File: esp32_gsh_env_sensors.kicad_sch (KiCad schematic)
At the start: 45 parts, among them J1 USB_C_Receptacle_USB2.0, Q1 SS8050, Q2 SS8050, SW1 EN, SW2 BOOT, U1 MP2359, U2 CH340G, U3 ESP32-WROOM-32E, U4 MH-Z19B, U5 BME280, Y1 12MHz

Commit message: Update schematics
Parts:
- added J3: Conn_01x05_Male, symbol Connector:Conn_01x05_Male
- added J5: Conn_01x04_Male, symbol Connector:Conn_01x04_Male
- J2: renamed from J?; value Conn_01x05_Female -> C50950
- J4: renamed from J?; value Conn_01x04_Female -> C2718488
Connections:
- net GND: now also C13.2, J4.3 (Pin_3); no longer C13.1, U4.7 (GND)
- net IO16/TXD: now also J2.3 (Pin_3); no longer U4.3 (TXD)
- net IO17/RXD: now also J2.2 (Pin_2); no longer U4.2 (RXD)
- net VBUS: now also C13.1, J4.4 (Pin_4); no longer C13.2, U4.6 (Vin)
- net MH-Z19B Vout: now reaches U4.1 (Vout)
- net MH-Z19B Vout: now also J3.1 (Pin_1)
- net MH-Z19B HD: now reaches U4.5 (HD)
- net MH-Z19B HD: now also J3.5 (Pin_5)
- net IO15/PWM: now reaches J4.1 (Pin_1)
- net IO15/PWM: now also U3.29 (GPIO5)
- net PWM renamed MH-Z19B PWM
- net MH-Z19B PWM: now also J5.1 (Pin_1); no longer U3.29 (GPIO5)
- new net MH-Z19B A0T: J5.2 (Pin_2)
- new net MH-Z19B GND: J5.3 (Pin_3), U4.7 (GND)
- new net MH-Z19B RXD: J3.2 (Pin_2), U4.2 (RXD)
- new net MH-Z19B SR: J3.4 (Pin_4)
- new net MH-Z19B TXD: J3.3 (Pin_3), U4.3 (TXD)
- new net MH-Z19B Vin: J5.4 (Pin_4), U4.6 (Vin)
- no-connect marks 30 -> 32
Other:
- moved on the sheet: C11, C12, C13, C14, C15, D3, J2, J4, R11, R12, U3, U4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

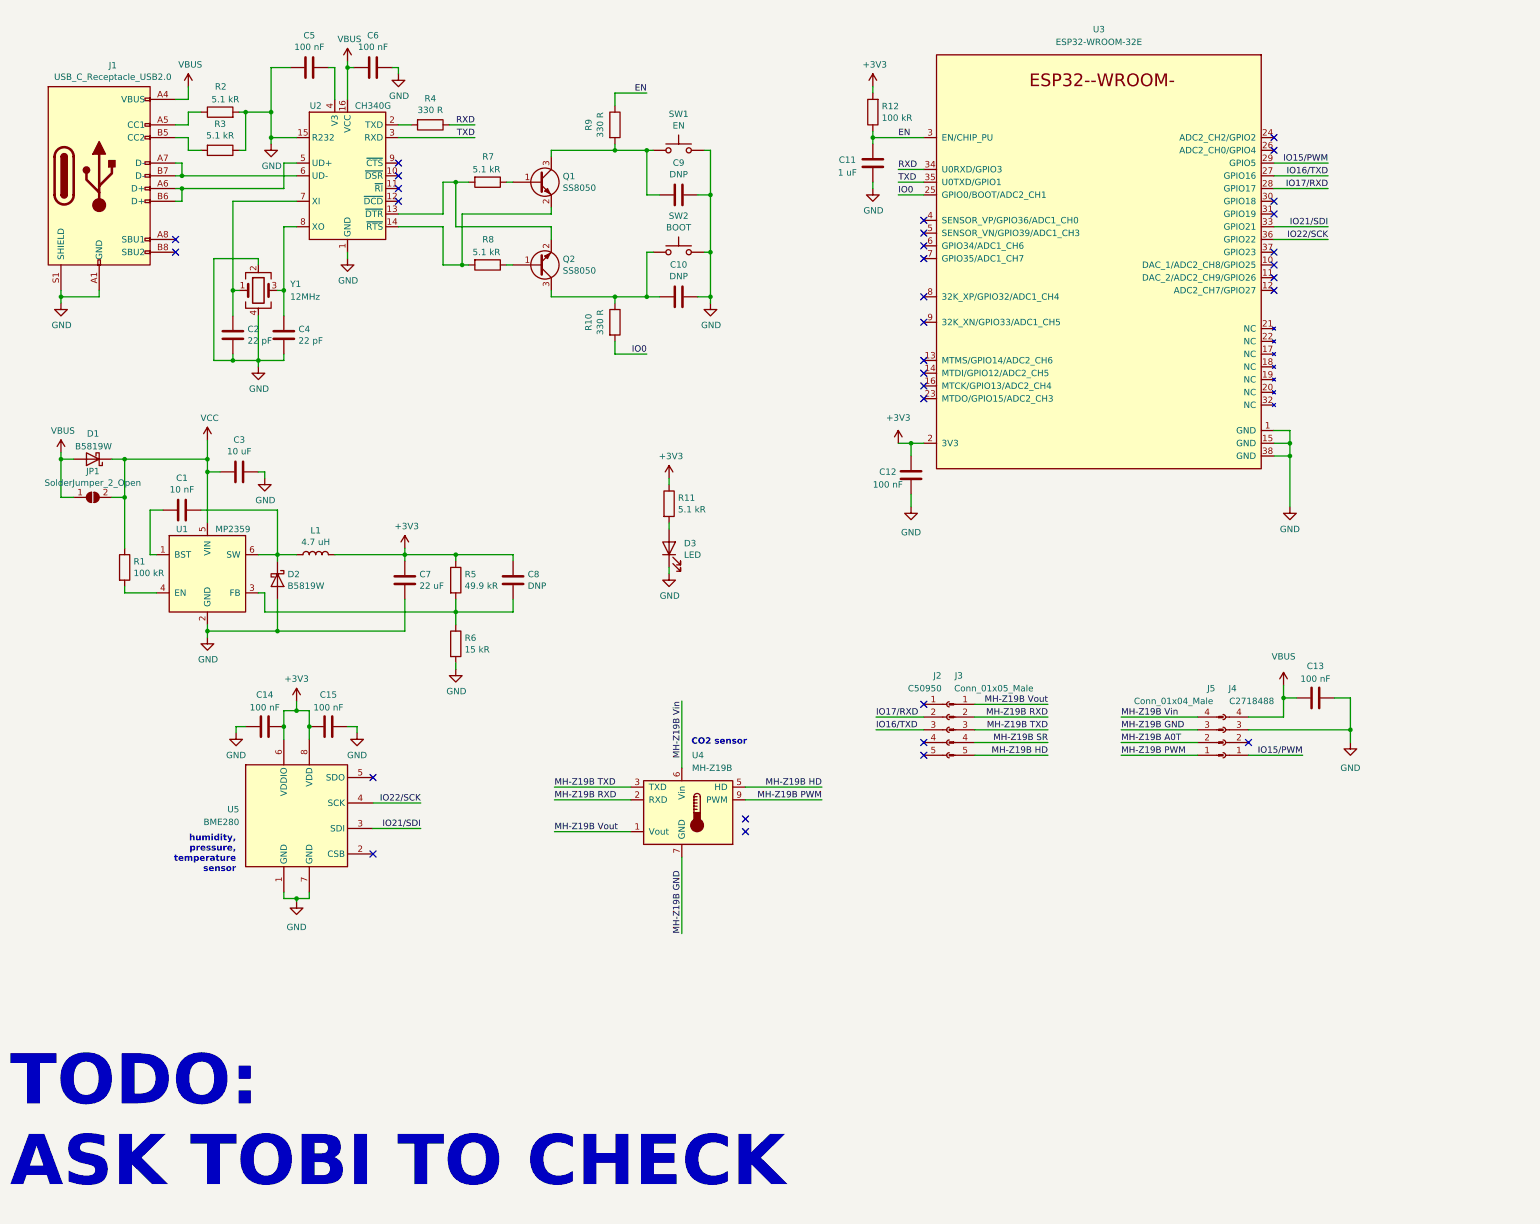
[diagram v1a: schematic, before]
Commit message: Multiple fixes, see below
- Change CH340G to 3.3V power source
- Fix floating pins (CSB, SDO) for BME280
- Add pull up resistors to BME280s SCK and SDI pins
- Fix naming of GPIO5 net (previously IO15/PWM, now IO5/PWM)
- Add switch to pull down MH-Z19Bs 'HD' pin for calibration
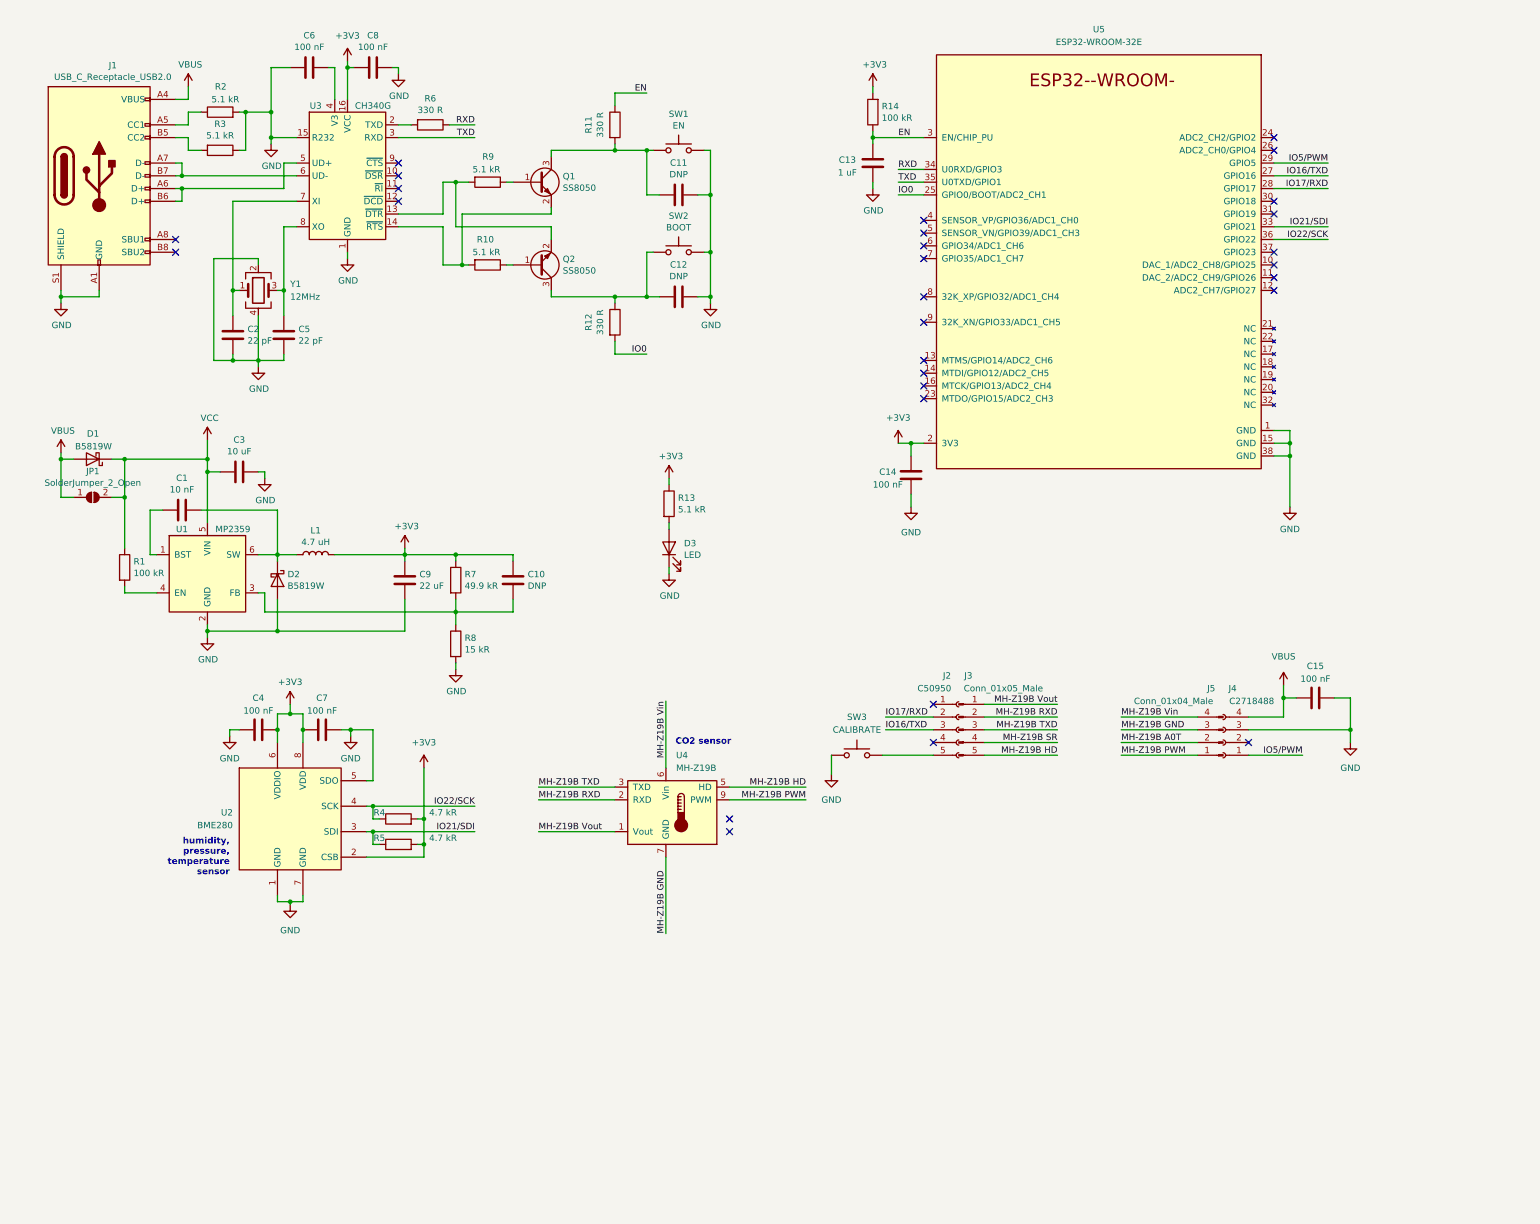
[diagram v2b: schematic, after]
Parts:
- added R4, R5: 4.7 kR, symbol Device:R
- added SW3: CALIBRATE, symbol Switch:SW_Push
- renumbered C8 to C10, C9 to C11, C10 to C12, C11 to C13, C12 to C14, C13 to C15, C14 to C4, C4 to C5, C5 to C6, C15 to C7, C6 to C8, C7 to C9, R8 to R10, R9 to R11, R10 to R12, R11 to R13, R12 to R14, R4 to R6, R5 to R7, R6 to R8, R7 to R9, U5 to U2, U2 to U3, U3 to U5
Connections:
- net +3V3: now also C8.2, U2.2 (CSB), U3.16 (VCC), R4.2, R5.2
- net GND: now also U2.5 (SDO), SW3.1
- net IO21/SDI: now also R5.1
- net IO22/SCK: now also R4.1
- net VBUS: no longer C8.2, U3.16 (VCC)
- net at J2.5 (Pin_5): now also SW3.2
- net IO15/PWM renamed IO5/PWM
- no-connect marks 32 -> 29
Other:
- note removed: "TODO: ASK TOBI TO CHECK"
- moved on the sheet: C4, C7, J2, J3, U2, U4

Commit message: Fix ch340 3.3V input; Add 5.1kR to protect ESP32; Add PWR_FLAG to schematics
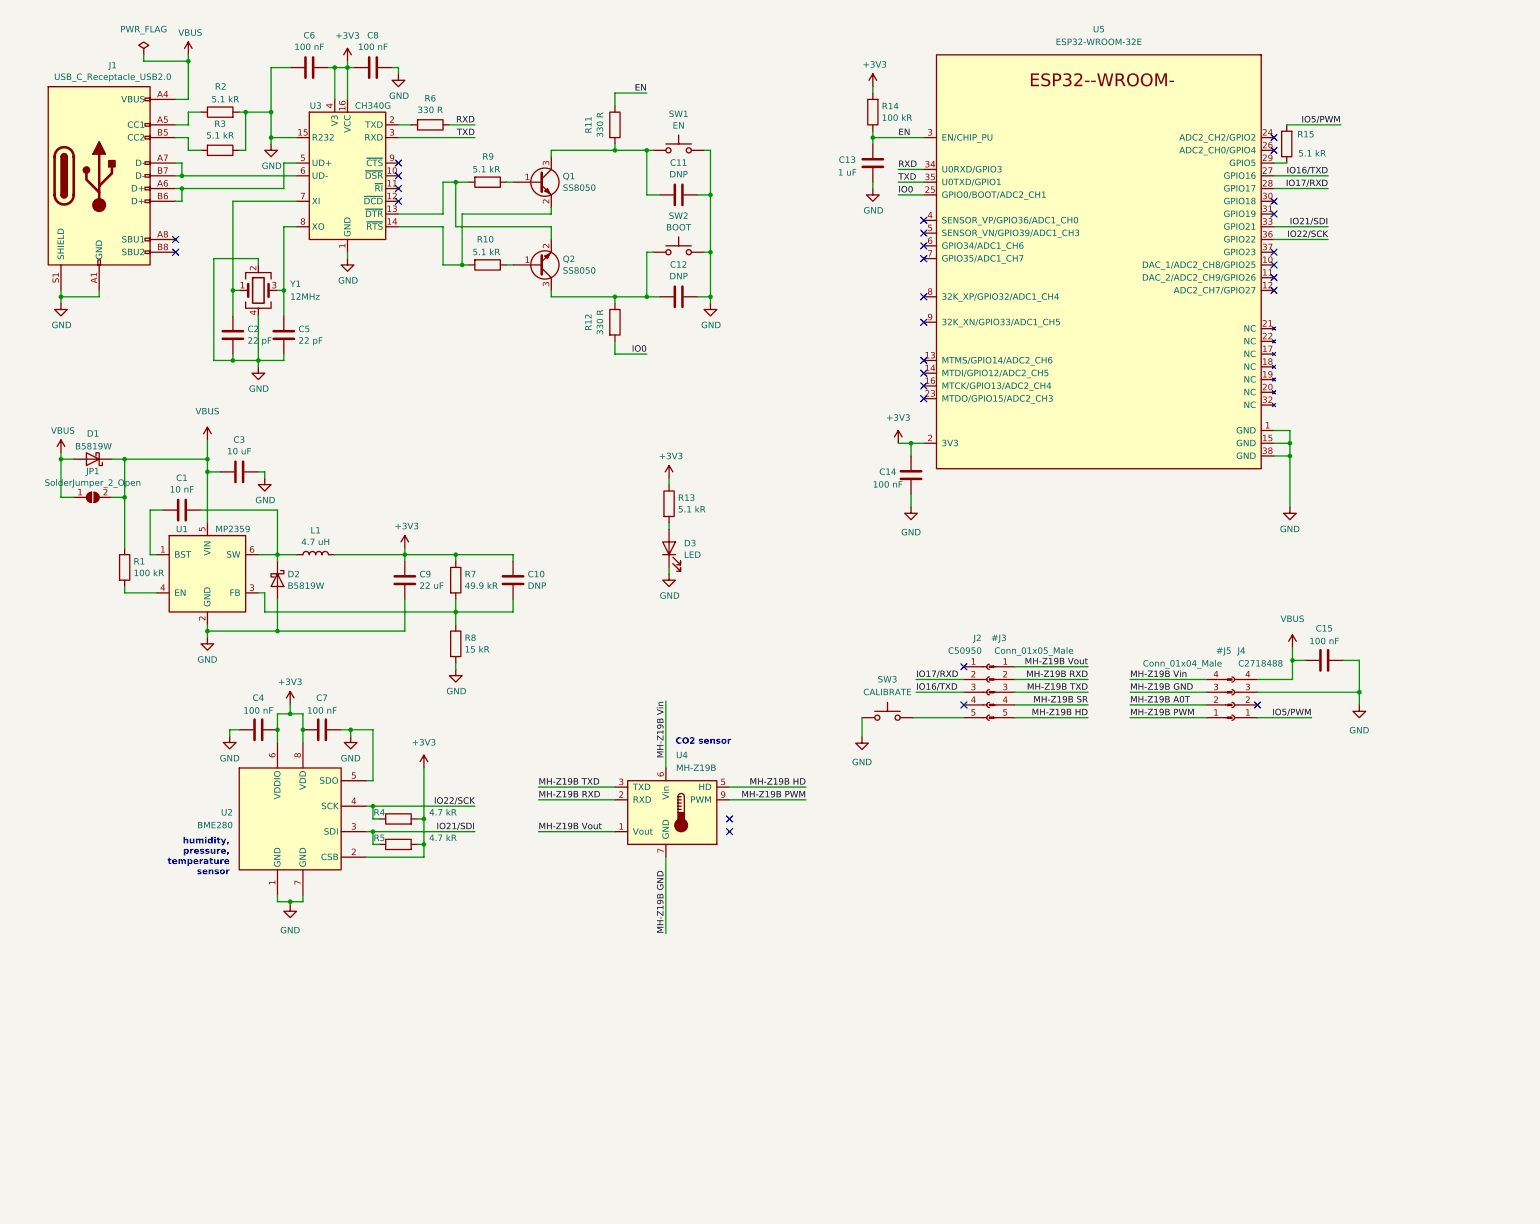
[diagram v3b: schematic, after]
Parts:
- added R15: 5.1 kR, symbol Device:R
- J2: LCSC (none) -> C50950
- J4: LCSC (none) -> C2718488
- renumbered J3 to #J3, J5 to #J5
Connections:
- net VCC is gone; now on net VBUS: C3.2, D1.1 (K), JP1.2 (B), R1.1, U1.5 (VIN)
- net +3V3: now also C6.1, U3.4 (V3)
- net IO5/PWM: now also R15.2; no longer U5.29 (GPIO5)
- new net: R15.1, U5.29 (GPIO5)
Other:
- moved on the sheet: C15, J2, J4, SW3

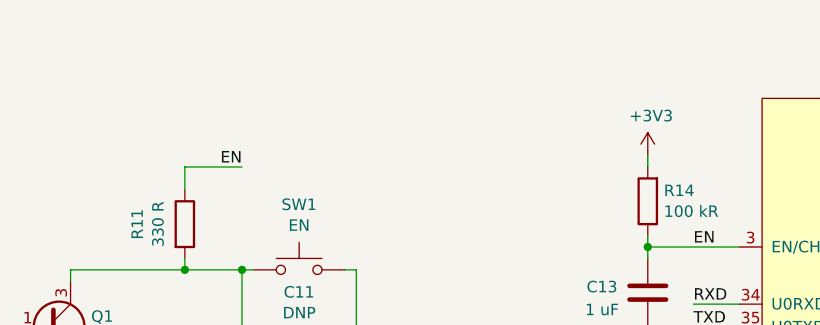
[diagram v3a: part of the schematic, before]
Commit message: Get schmeatics ready for layouting
- Add OSHW logo
- Add manufacturing mounting holes
- Assign footprints
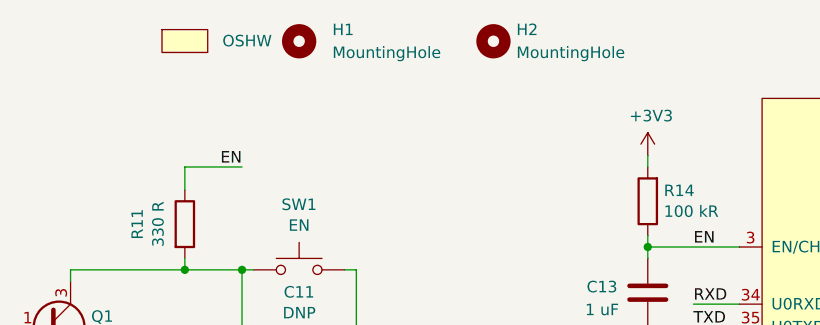
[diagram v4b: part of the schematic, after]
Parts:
- added H1, H2: MountingHole, ToolingHole:ToolingHole_JLCSMT, symbol Mechanical:MountingHole
- added I1: OSHW, Symbol:OSHW-Logo2_9.8x8mm_SilkScreen, symbol Icon:Icon
- C10, C11, C12: footprint Capacitor_SMD:C_0402_1005Metric -> Capacitor_SMD:C_0402_1005Metric_Pad0.74x0.62mm_HandSolder
- C14, C15, C4, C7: footprint (none) -> Capacitor_SMD:C_0402_1005Metric
- J2: footprint (none) -> Connector_PinSocket_2.54mm:PinSocket_1x05_P2.54mm_Vertical
- J4: footprint (none) -> Connector_PinSocket_2.54mm:PinSocket_1x04_P2.54mm_Vertical
- R15, R4, R5: footprint (none) -> Resistor_SMD:R_0402_1005Metric
- SW3: footprint (none) -> Button_Switch_SMD:SW_Push_SPST_NO_Alps_SKRK

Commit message: Add LSCS part numbers where available
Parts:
- C14, C15, C4, C7: LCSC (none) -> C1525
- R10, R13, R2, R3, R9: LCSC C25905 -> C25905
- R15: LCSC (none) -> C25905
- R4, R5: LCSC (none) -> C25900
- SW3: LCSC (none) -> C115357
- U2: LCSC (none) -> C92489
- U5: LCSC (none) -> C701343
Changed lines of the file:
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@@
+      (effects (font (size 1.27 1.27)) hide)
+    )
+    (property "LCSC" "C25900" (id 4) (at 86.36 179.07 0)
       (effects (font (size 1.27 1.27)) hide)
     )
@@
       (effects (font (size 1.27 1.27)) hide)
     )
+    (property "LCSC" "C25905" (id 4) (at 263.525 39.37 0)
+      (effects (font (size 1.27 1.27)) hide)
+    )
     (pin "1")
     (pin "2")
@@
       (effects (font (size 1.27 1.27)) hide)
     )
+    (property "LCSC" "C115357" (id 4) (at 183.896 153.797 0)
+      (effects (font (size 1.27 1.27)) hide)
+    )
     (pin "1")
     (pin "2")
@@
     )
     (property "Datasheet" "https://www.espressif.com/sites/default/files/documentation/esp32-wroom-32e_esp32-wroom-32ue_datasheet_en.pdf" (id 3) (at 235.585 63.5 0)
+      (effects (font (size 1.27 1.27)) hide)
+    )
+    (property "LCSC" "C701343" (id 4) (at 225.425 63.5 0)
       (effects (font (size 1.27 1.27)) hide)
     )
@@
       (effects (font (size 1.27 1.27)) hide)
     )
+    (property "LCSC" "C25900" (id 4) (at 86.36 173.99 0)
+      (effects (font (size 1.27 1.27)) hide)
+    )
     (pin "1")
     (pin "2")
@@
       (effects (font (size 1.27 1.27)) hide)
     )
-    (property "LCSC" " C25905" (id 4) (at 50.8 40.64 0)
+    (property "LCSC" "C25905" (id 4) (at 50.8 40.64 0)
       (effects (font (size 1.27 1.27)) hide)
     )
@@
       (effects (font (size 1.27 1.27)) hide)
     )
-    (property "LCSC" " C25905" (id 4) (at 50.8 33.02 0)
+    (property "LCSC" "C25905" (id 4) (at 50.8 33.02 0)
       (effects (font (size 1.27 1.27)) hide)
     )
@@
       (effects (font (size 1.27 1.27)) hide)
     )
+    (property "LCSC" "C1525" (id 4) (at 71.12 156.21 0)
+      (effects (font (size 1.27 1.27)) hide)
+    )
     (pin "1")
     (pin "2")
@@
       (effects (font (size 1.27 1.27)) hide)
     )
+    (property "LCSC" "C1525" (id 4) (at 188.595 105.41 0)
+      (effects (font (size 1.27 1.27)) hide)
+    )
     (pin "1")
     (pin "2")
@@
       (effects (font (size 1.27 1.27)) hide)
     )
-    (property "LCSC" " C25905" (id 4) (at 104.14 63.5 0)
+    (property "LCSC" "C25905" (id 4) (at 104.14 63.5 0)
       (effects (font (size 1.27 1.27)) hide)
     )
@@
       (effects (font (size 1.27 1.27)) hide)
     )
-    (property "LCSC" " C25905" (id 4) (at 140.335 111.125 0)
+    (property "LCSC" "C25905" (id 4) (at 140.335 111.125 0)
       (effects (font (size 1.27 1.27)) hide)
     )
@@
       (effects (font (size 1.27 1.27)) hide)
     )
-    (property "LCSC" " C25905" (id 4) (at 104.14 46.99 0)
+    (property "LCSC" "C25905" (id 4) (at 104.14 46.99 0)
       (effects (font (size 1.27 1.27)) hide)
     )
@@
     )
     (property "Datasheet" "~" (id 3) (at 58.42 156.21 0)
+      (effects (font (size 1.27 1.27)) hide)
+    )
+    (property "LCSC" "C1525" (id 4) (at 58.42 156.21 0)
       (effects (font (size 1.27 1.27)) hide)
     )
@@
       (effects (font (size 1.27 1.27)) hide)
     )
+    (property "LCSC" "C1525" (id 4) (at 271.018 142.367 0)
+      (effects (font (size 1.27 1.27)) hide)
+    )
     (pin "1")
     (pin "2")
@@
       (effects (font (size 1.27 1.27)) hide)
     )
-    (property "Datasheet" "" (id 3) (at 109.22 126.365 0)
+    (property "Datasheet" "~" (id 3) (at 109.22 126.365 0)
       (effects (font (size 1.27 1.27)) hide)
     )
@@
       (effects (font (size 1.27 1.27)) hide)
     )
+    (property "LCSC" "C92489" (id 4) (at 64.77 173.99 0)
+      (effects (font (size 1.27 1.27)) hide)
+    )

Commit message: Fix title
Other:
- title: GSH ESP32 environment sensor -> GSH ESP32 environment sensors
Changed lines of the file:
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@@
   (paper "A4")
   (title_block
-    (title "GSH ESP32 environment sensor")
+    (title "GSH ESP32 environment sensors")
     (date "2022-02-24")
     (rev "A")

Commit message: Fix LED and MH-Z19B footprints
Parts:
- D3: footprint LED_SMD:LED_0603_1608Metric_Castellated -> LED_SMD:LED_0603_1608Metric
- U4: footprint sensor_Carbon_dioxide:mh-z19b -> mh-z19b:Winsen_MH-Z19B
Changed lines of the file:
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@@
       (effects (font (size 1.27 1.27)) (justify left))
     )
-    (property "Footprint" "sensor_Carbon_dioxide:mh-z19b" (id 2) (at 139.7 189.23 0)
+    (property "Footprint" "mh-z19b:Winsen_MH-Z19B" (id 2) (at 139.7 189.23 0)
       (effects (font (size 1.27 1.27)) hide)
     )
@@
       (effects (font (size 1.27 1.27)) (justify right))
     )
-    (property "Footprint" "LED_SMD:LED_0603_1608Metric_Castellated" (id 2) (at 140.335 120.015 0)
+    (property "Footprint" "LED_SMD:LED_0603_1608Metric" (id 2) (at 140.335 120.015 0)
       (effects (font (size 1.27 1.27)) hide)
     )
@@
     )
     (path "/7a78444a-9bdf-4ec4-8b89-d938f2327fb9"
-      (reference "D3") (unit 1) (value "LED") (footprint "LED_SMD:LED_0603_1608Metric_Castellated")
+      (reference "D3") (unit 1) (value "LED") (footprint "LED_SMD:LED_0603_1608Metric")
     )
     (path "/389a456e-233e-44fa-b748-df37a931fcce"
@@
     )
     (path "/48e524c1-95e4-45a2-a85b-edc3dddcf78f"
-      (reference "U4") (unit 1) (value "MH-Z19B") (footprint "sensor_Carbon_dioxide:mh-z19b")
+      (reference "U4") (unit 1) (value "MH-Z19B") (footprint "mh-z19b:Winsen_MH-Z19B")
     )
     (path "/19e32940-9c09-4bdc-94e1-dfe7f5bac49c"
